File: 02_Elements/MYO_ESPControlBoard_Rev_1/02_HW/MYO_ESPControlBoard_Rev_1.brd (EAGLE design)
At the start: 72 x 49 mm, 47 parts, among them X2 332-06

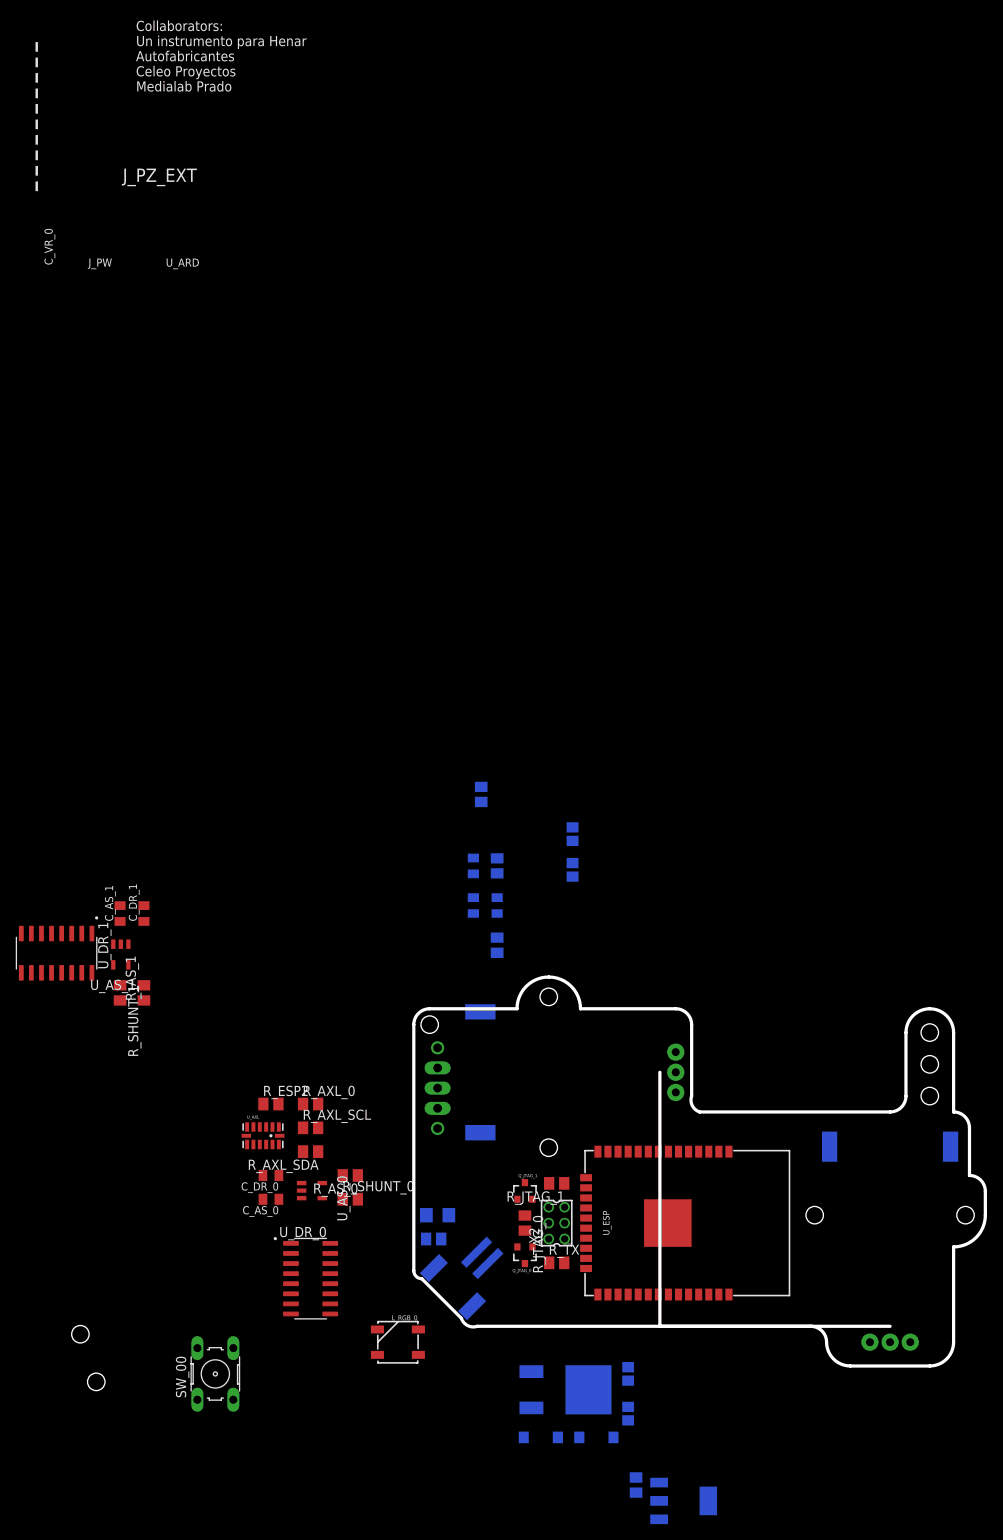
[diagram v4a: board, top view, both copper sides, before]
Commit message: Updated Dimension and Layout MYO_ESPControlBoard_Rev_1
Changes on MYO_ESPControlBoard_Rev_1:

- New Dimensions and Layout
- Changed Motor + Bracket Footprint
- Changed User Tactile Switch
- Added BOM in .txt format
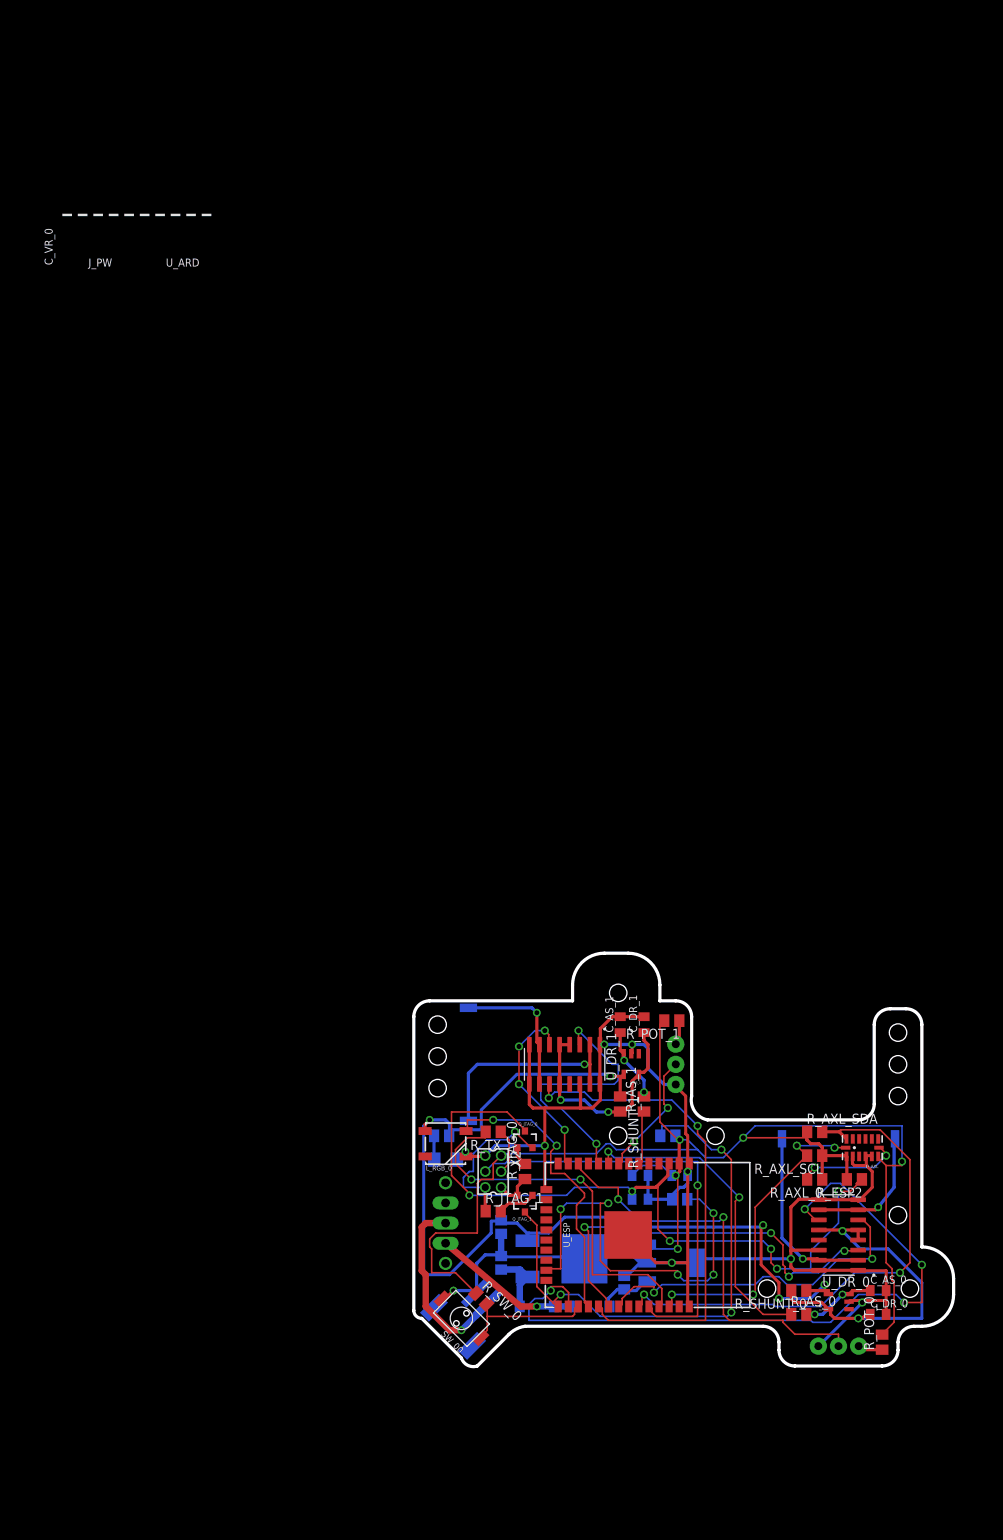
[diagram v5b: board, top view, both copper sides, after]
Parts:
- removed R_ESP1: 5KOhm, adafruit:M0805
- added R_POT_0, R_POT_1: ???, adafruit:M0805
- SW_00: value (none) -> SWITCH-MOMENTARY-2TACTILE-SWITCH-SMD-RIGHT-ANGLE; device switch-omron:B3F-10XX -> SparkFun-Electromechanical:TACTILE_SWITCH-SMD-RIGHT-ANGLE
- moved C_DR_0 78.5 mm to (58.5, 6.50), turned to 0 degrees
- moved C_AS_0 77.4 mm to (58.5, 9.50), turned to 0 degrees
- moved U_AXL 75.5 mm to (56.5, 27.5), turned to 180 degrees
- moved R_ESP2 74.1 mm to (55.5, 23.5), turned to 180 degrees
- moved U_AS_0 68.0 mm to (53.5, 8.00), turned to 90 degrees
- moved U_DR_0 66.7 mm to (53.5, 16.5), turned to 180 degrees
- moved U_AS_1 66.0 mm to (27.5, 38.0)
- moved U_DR_1 65.5 mm to (19.0, 38.0)
- moved C_AS_1 64.5 mm to (26.0, 43.0)
- moved C_DR_1 64.5 mm to (29.0, 43.0)
- moved R_AS_1 64.5 mm to (29.0, 33.0)
- moved R_SHUNT_1 64.5 mm to (26.0, 33.0)
- moved R_AXL_0 64.2 mm to (50.5, 23.5), turned to 180 degrees
- moved R_AXL_SCL 63.6 mm to (50.5, 26.5), turned to 180 degrees
- moved R_AXL_SDA 63.5 mm to (50.5, 29.5), turned to 0 degrees
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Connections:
- removed net SWTAC_0: R_ESP1.1
- new net N$2: MOTPOT_0.3V3, R_POT_0.1
- new net N$3: MOTPOT_1.3V3, R_POT_1.1
- net 3V3: now also R_POT_0.2, R_POT_1.2; no longer MOTPOT_0.3V3, MOTPOT_1.3V3
- net GND: now also SW_00.2; no longer R_ESP1.2, SW_00.1
- net SW_0: now also SW_00.1; no longer SW_00.3
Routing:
- net GND: track 0.00 -> 238.1 mm, vias 0 -> 9
- net 3V3: track 0.00 -> 184.7 mm, vias 0 -> 5
- net 5V: track 0.00 -> 125.8 mm, vias 0 -> 5
- net EN: track 0.00 -> 93.5 mm, vias 0 -> 6
- net MOT_EN_0: track 0.00 -> 89.3 mm, vias 0 -> 4
- net GPIO0(R): track 0.00 -> 69.2 mm, vias 0 -> 3
- net SDA: track 0.00 -> 65.4 mm, vias 0 -> 2
- net MOT_EN_1: track 0.00 -> 62.2 mm, vias 0 -> 2
- net RXD: track 0.00 -> 53.7 mm, vias 0 -> 1
- net MPOT_0: track 0.00 -> 52.1 mm, vias 0 -> 2
- net GPIO15(R): track 0.00 -> 51.7 mm, vias 0 -> 5
- net MOT_A_0: track 0.00 -> 51.6 mm, vias 0 -> 4
- net TXD: track 0.00 -> 48.1 mm, vias 0 -> 2
- net VCC_VR_0: track 0.00 -> 44.0 mm, vias 0 -> 2
- net MOT_B_0: track 0.00 -> 42.8 mm, vias 0 -> 2
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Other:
- board size 72 x 49 mm -> 68 x 52.1 mm
- board text removed: "Collaborators: Un instrumento para Henar Autofabricantes Celeo Proyectos Medialab Prado"
- board text removed: "J_PZ_EXT"
